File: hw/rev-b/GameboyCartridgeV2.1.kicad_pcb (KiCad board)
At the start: 6 copper layers, 52.8 x 61.2 mm, 148 parts, among them J1 USB_C_Receptacle_USB2.0, J2 Micro_SD_Card_Det2, J4 Conn_01x06, J5 CartBus, Q1 CJ2302, Q101 SIA975DJ-T1-GE3, Q102 2N7002, SW1 SW_Push, SW2 SW_Push, U1 USBLC6-2P6, U101 TPS2116DRLR, U102 TPS2553DBVR, U103 TPS63802DLAR, U104 ESP32-C3-MINI-1U-N4, U105 SN74LVC1G125DBVR, U106 SN74LVC3G34DCTR, U107 CH334P, U108 TLV3012BIDBVR, U109 TLV431BIDBZR, U2 W25Q16JVSSIQ, U3 RP2350_80QFN, U4 W956A8MBYA5I, U5 MCP79510, U6 AP2112K-3.3, U7 TXB0108PW, Y1 12MHz, Y101 12MHz 10pF 10ppm, Y2 32.768kHz

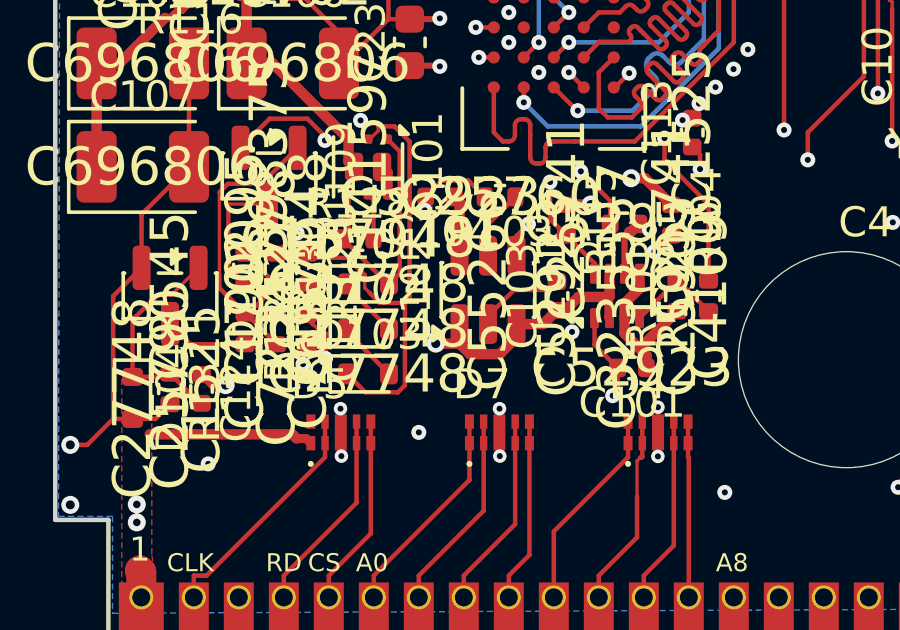
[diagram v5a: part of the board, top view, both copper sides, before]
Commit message: routing: finisher fixes (via clearance, fan-out BFS, direct connections), F.Cu GND pour; 11 open; logbook
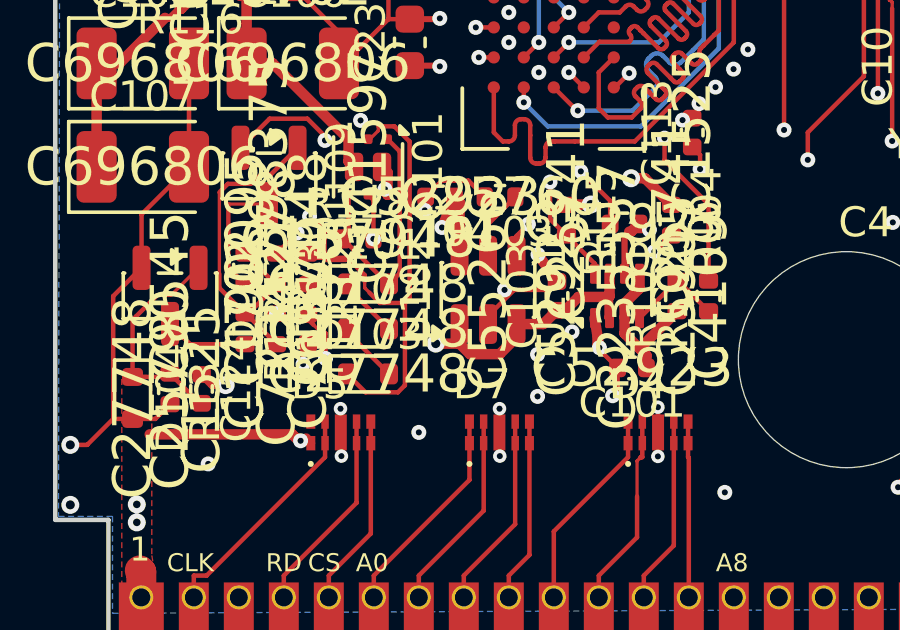
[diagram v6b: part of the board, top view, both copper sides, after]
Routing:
- net VCC: track 65.9 -> 77.6 mm, vias 10 -> 11
- net GND: track 207.6 -> 218.0 mm, vias 199 -> 204
- net /Radio/REG_G: track 18.0 -> 22.9 mm, vias 0 -> 2
- net VLIM: track 3.03 -> 6.93 mm, vias 0 -> 2

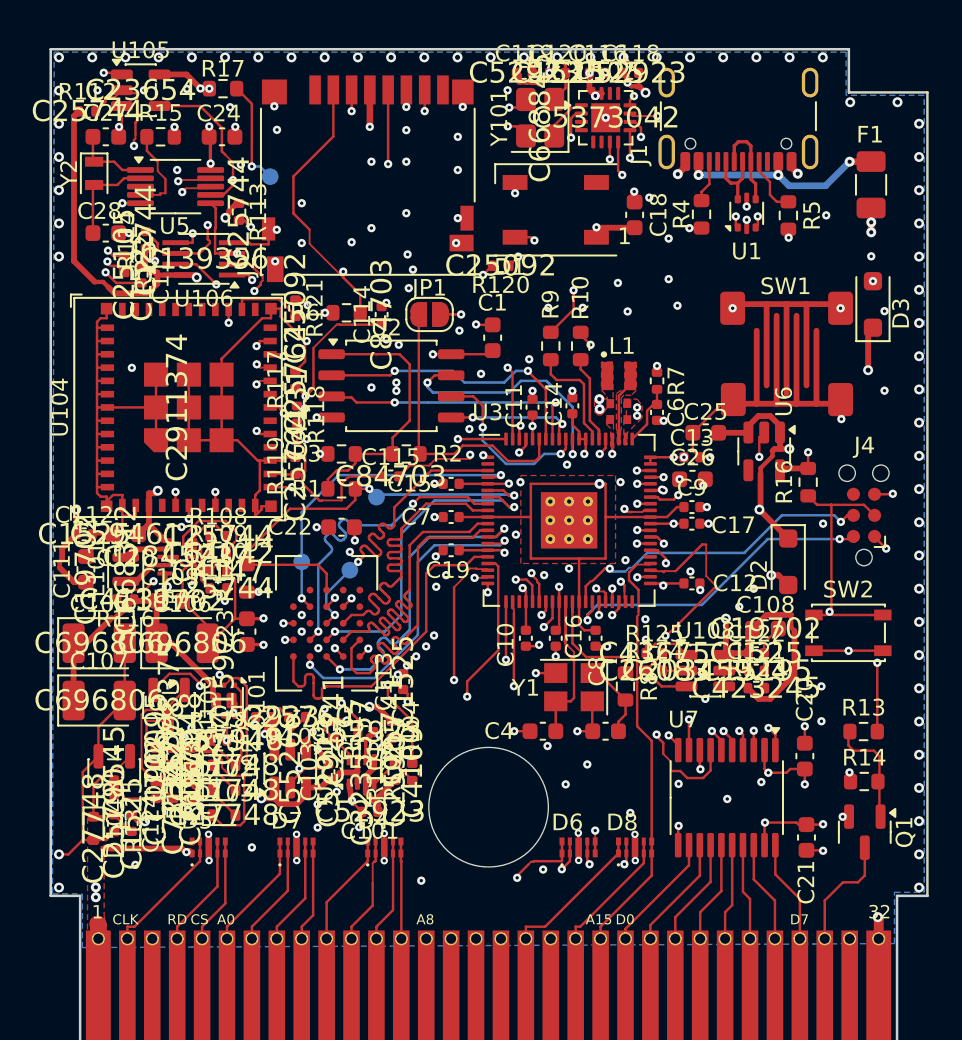
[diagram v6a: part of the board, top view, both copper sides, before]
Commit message: routing pass 3: slow Croco nets re-routed with the stuck ones, orphan +5V plane removed; 7 open
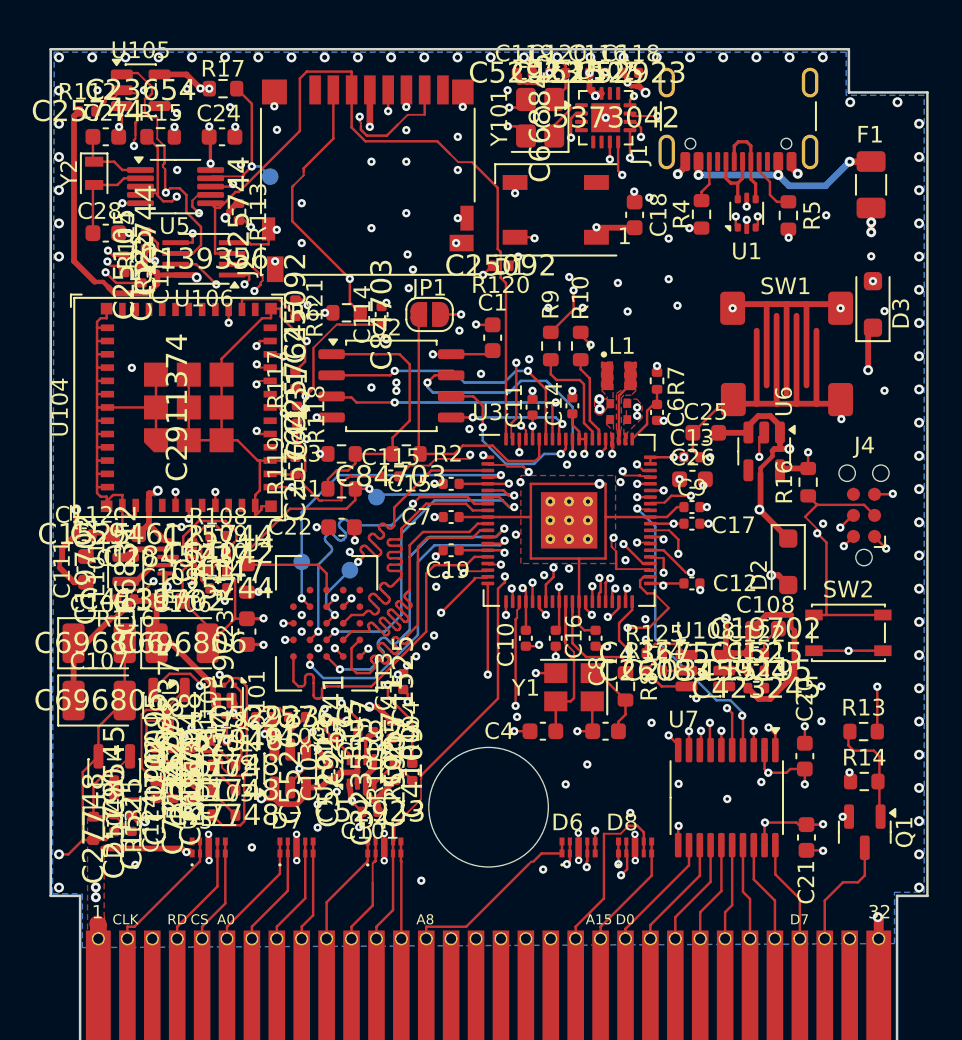
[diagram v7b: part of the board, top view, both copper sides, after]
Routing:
- net DEBUG_UART_TX: track 17.2 -> 58.9 mm
- net RTC_CS: track 5.47 -> 43.9 mm, vias 0 -> 2
- net GB_A3: track 6.15 -> 32.9 mm, vias 0 -> 1
- net GB_A7: track 30.4 -> 5.87 mm, vias 1 -> 0
- net GB_A12: track 8.85 -> 25.5 mm, vias 0 -> 2
- net GB_A15: track 25.5 -> 36.8 mm, vias 0 -> 1
- net DATA_BUS0: track 1.85 -> 13.0 mm, vias 1 -> 2
- net GB_RD: track 47.6 -> 37.6 mm
- net GB_A8: track 32.5 -> 41.6 mm, vias 2 -> 1
- net SPI_MOSI: track 38.3 -> 46.6 mm, vias 4 -> 0
- net GB_A11: track 31.8 -> 26.7 mm, vias 3 -> 2
- net BUS_RST: track 25.1 -> 30.0 mm
- net Net-(U5-MFP): track 13.5 -> 9.25 mm, vias 2 -> 1
- net SPI_MISO: track 48.1 -> 51.9 mm, vias 3 -> 4
- net DATA_BUS7: track 19.7 -> 23.6 mm
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- removed copper zone on In4.Cu, net +5V

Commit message: routing: finisher base raster for 0.15 mm tracks; 3 open
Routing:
- net GND: track 218.0 -> 229.7 mm, vias 204 -> 210
- net /Radio/PG_SENSE: track 4.31 -> 10.4 mm, vias 0 -> 2
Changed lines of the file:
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@@
 	)
 	(segment
+		(start 118.7875 71.7)
+		(end 118.660015 71.854102)
+		(width 0.35)
+		(layer "F.Cu")
+		(net "GND")
+	)
+	(segment
 		(start 132.036471 99)
 		(end 132.511471 98.525)
@@
 	)
 	(segment
+		(start 118.7875 70.7)
+		(end 117.808038 70.700958)
+		(width 0.15)
+		(layer "F.Cu")
+		(net "GND")
+	)
+	(segment
 		(start 121.1797 93.2998)
 		(end 120.8799 93)
@@
 	)
 	(segment
+		(start 119.1524 105.0054)
+		(end 119.408037 105.250958)
+		(width 0.15)
+		(layer "F.Cu")
+		(net "GND")
+	)
+	(segment
 		(start 151.175 110.362)
 		(end 151.175 110.3625)
@@
 	)
 	(segment
+		(start 117.708038 70.800958)
+		(end 117.708038 70.900958)
+		(width 0.15)
+		(layer "F.Cu")
+		(net "GND")
+	)
+	(segment
 		(start 151.175 110.362)
 		(end 151.175 110.3625)
@@
 	)
 	(segment
+		(start 117.808038 70.700958)
+		(end 117.708038 70.800958)
+		(width 0.15)
+		(layer "F.Cu")
+		(net "GND")
+	)
+	(segment
 		(start 151.855 73.195)
 		(end 151.85 73.2)
@@
 	)
 	(segment
+		(start 157.208038 97.325958)
+		(end 156.612769 97.401157)
+		(width 0.35)
+		(layer "F.Cu")
+		(net "GND")
+	)
+	(segment
 		(start 136.942464 92.6)
 		(end 136.571232 92.971232)
@@
 	)
 	(segment
+		(start 117.708038 70.900958)
+		(end 117.508038 71.100957)
+		(width 0.15)
+		(layer "F.Cu")
+		(net "GND")
+	)
+	(segment
 		(start 127.808 106.888)
 		(end 127.808 106.8885)
@@
 	)
 	(via
+		(at 159.35 98.65)
+		(size 0.5)
+		(drill 0.2)
+		(layers "F.Cu" "B.Cu")
+		(net "GND")
+	)
+	(via
 		(at 131.9623 109.2775)
 		(size 0.5)
@@
 	)
 	(via
+		(at 156.612769 97.401157)
+		(size 0.5)
+		(drill 0.2)
+		(layers "F.Cu" "B.Cu")
+		(net "GND")
+	)
+	(via
 		(at 121.883038 62.916285)
 		(size 0.6)
@@
 	)
 	(via
+		(at 119.408037 105.250958)
+		(size 0.5)
+		(drill 0.2)
+		(layers "F.Cu" "B.Cu")
+		(net "GND")
+	)
+	(via
 		(at 165.683038 82.916285)
 		(size 0.6)
@@
 	)
 	(via
+		(at 118.660015 71.854102)
+		(size 0.5)
+		(drill 0.2)
+		(layers "F.Cu" "B.Cu")
+		(net "GND")
+	)
+	(via
 		(at 115.883038 62.916285)
 		(size 0.6)
@@
 	)
 	(via
+		(at 117.84 101.65)
+		(size 0.5)
+		(drill 0.2)
+		(layers "F.Cu" "B.Cu")
+		(net "GND")
+	)
+	(via
 		(at 146.788 63.8213)
 		(size 0.5)
@@
 	)
 	(via
+		(at 117.508038 71.100957)
+		(size 0.5)
+		(drill 0.2)
+		(layers "F.Cu" "B.Cu")
+		(net "GND")
+	)
+	(via
 		(at 142.2 81.1)
 		(size 0.5)
@@
 	)
 	(segment
+		(start 159.35 98.65)
+		(end 158.108038 97.400958)
+		(width 0.35)
+		(layer "In2.Cu")
+		(net "GND")
+	)
+	(segment
+		(start 117.508038 71.100957)
+		(end 118.258038 71.850957)
+		(width 0.35)
+		(layer "In2.Cu")
+		(net "GND")
+	)
+	(segment
+		(start 119.358038 103.950958)
+		(end 119.408037 104.000958)
+		(width 0.35)
+		(layer "In2.Cu")
+		(net "GND")
+	)
+	(segment
+		(start 158.108038 97.400958)
+		(end 156.612769 97.401157)
+		(width 0.35)
+		(layer "In2.Cu")
+		(net "GND")
+	)
+	(segment
 		(start 129.858038 109.200958)
 		(end 129.908038 109.150958)
@@
 	)
 	(segment
+		(start 118.258038 71.850957)
+		(end 118.660015 71.854102)
+		(width 0.35)
+		(layer "In2.Cu")
+		(net "GND")
+	)
+	(segment
+		(start 119.408037 104.000958)
+		(end 119.408037 105.250958)
+		(width 0.35)
+		(layer "In2.Cu")
+		(net "GND")
+	)
+	(segment
 		(start 129.308038 107.750958)
 		(end 129.458037 107.900958)
@@
 	)
 	(segment
+		(start 117.84 101.65)
+		(end 119.358038 103.150958)
+		(width 0.35)
+		(layer "In2.Cu")
+		(net "GND")
+	)
+	(segment
 		(start 129.308038 106.700958)
 		(end 129.308038 107.750958)
@@
 	)
 	(segment
+		(start 119.358038 103.150958)
+		(end 119.358038 103.950958)
+		(width 0.35)
+		(layer "In2.Cu")
+		(net "GND")
+	)
+	(segment
 		(start 129.458037 109.300958)
 		(end 129.558038 109.200958)
@@
 		(net "/Radio/PG_SENSE")
 	)
+	(segment
+		(start 151.670538 100.800957)
+		(end 151.633016 101.700174)
+		(width 0.15)
+		(layer "F.Cu")
+		(net "/Radio/PG_SENSE")
+	)
+	(via
+		(at 151.633016 101.700174)
+		(size 0.5)
+		(drill 0.2)
+		(layers "F.Cu" "B.Cu")
+		(net "/Radio/PG_SENSE")
+	)
+	(via
+		(at 156.388038 100.900957)
+		(size 0.5)
+		(drill 0.2)
+		(layers "F.Cu" "B.Cu")
+		(net "/Radio/PG_SENSE")
+	)
+	(segment
+		(start 151.633016 101.700174)
+		(end 151.758038 101.550958)
+		(width 0.15)
+		(layer "In2.Cu")
+		(net "/Radio/PG_SENSE")
+	)
+	(segment
+		(start 151.858038 101.200958)
+		(end 152.158038 100.900958)
+		(width 0.15)
+		(layer "In2.Cu")
+		(net "/Radio/PG_SENSE")
+	)
+	(segment
+		(start 152.158038 100.900958)
+		(end 156.388038 100.900957)
+		(width 0.15)
+		(layer "In2.Cu")
+		(net "/Radio/PG_SENSE")
+	)
+	(segment
+		(start 151.858038 101.250958)
+		(end 151.858038 101.200958)
+		(width 0.15)
+		(layer "In2.Cu")
+		(net "/Radio/PG_SENSE")
+	)
+	(segment
+		(start 151.758038 101.550958)
+		(end 151.758038 101.400958)
+		(width 0.15)
+		(layer "In2.Cu")
+		(net "/Radio/PG_SENSE")
+	)
+	(segment
+		(start 151.758038 101.400958)
+		(end 151.808038 101.350957)
+		(width 0.15)
+		(layer "In2.Cu")
+		(net "/Radio/PG_SENSE")
+	)
+	(segment
+		(start 151.808038 101.350957)
+		(end 151.808038 101.300958)
+		(width 0.15)
+		(layer "In2.Cu")
+		(net "/Radio/PG_SENSE")
+	)
+	(segment
+		(start 151.808038 101.300958)
+		(end 151.858038 101.250958)
+		(width 0.15)
+		(layer "In2.Cu")
+		(net "/Radio/PG_SENSE")
+	)
